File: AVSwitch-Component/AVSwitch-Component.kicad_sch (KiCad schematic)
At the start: 11 parts, among them J1 Conn_01x35_Pin, U1 SN74CBT3244PW

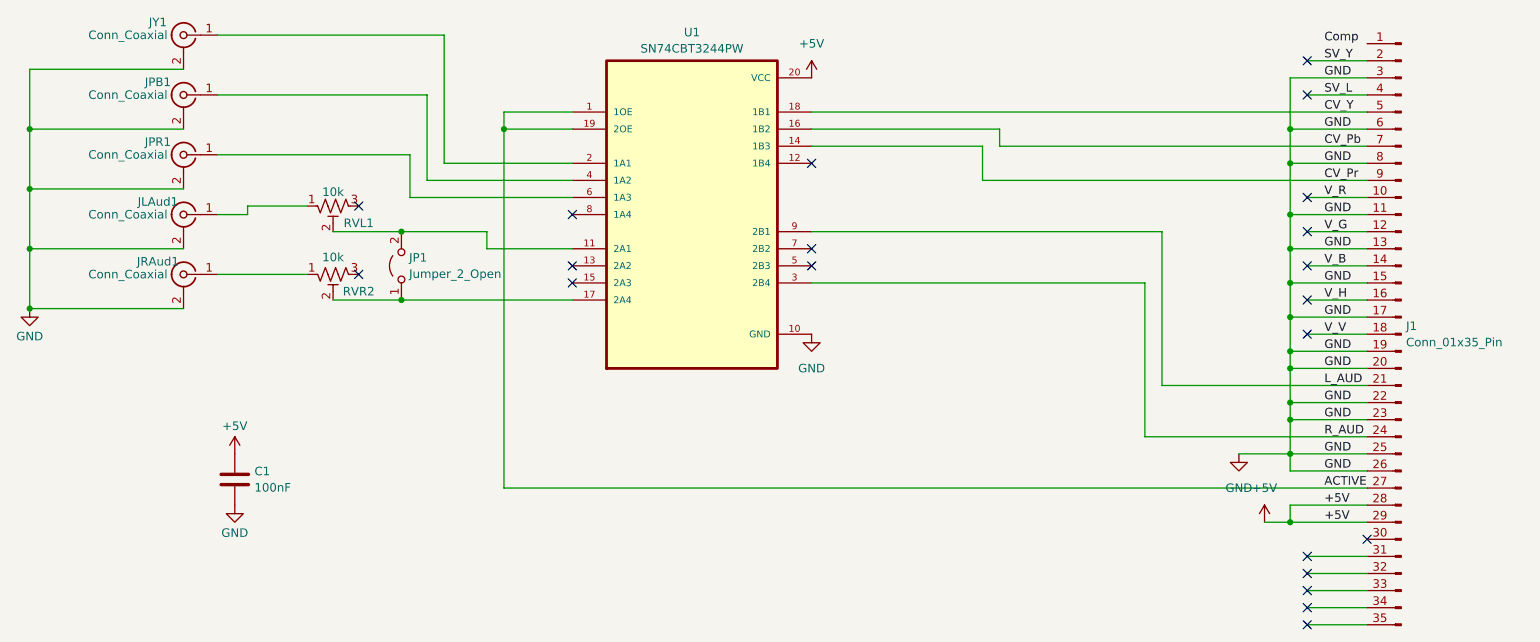
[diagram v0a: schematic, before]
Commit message: Add files via upload
New version with better footprint and ground isolation.
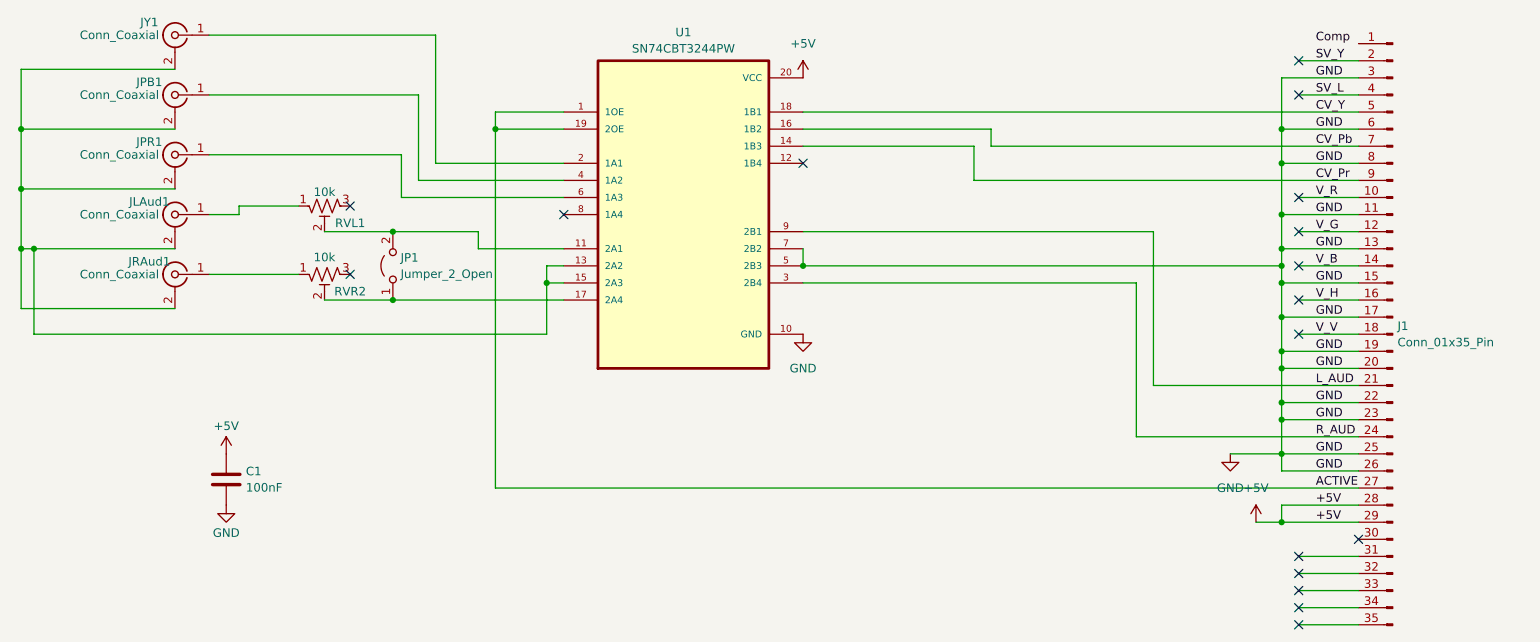
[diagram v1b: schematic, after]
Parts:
- U1: footprint Package_SO:TSSOP-20_4.4x6.5mm_P0.65mm -> Package_SO:SOIC-20W_7.5x12.8mm_P1.27mm
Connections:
- net GND: now also U1.5 (2B3), U1.7 (2B2); no longer JLAud1.2 (Ext), JPB1.2 (Ext), JPR1.2 (Ext), JRAud1.2 (Ext), JY1.2 (Ext)
- net at U1.13 (2A2): now also JLAud1.2 (Ext), JPB1.2 (Ext), JPR1.2 (Ext), JRAud1.2 (Ext), JY1.2 (Ext), U1.15 (2A3)
- no-connect marks 21 -> 17
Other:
- moved on the sheet: C1, J1, JLAud1, JP1, JPB1, JPR1, JRAud1, JY1, RVL1, RVR2, U1
